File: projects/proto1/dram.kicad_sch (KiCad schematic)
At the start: 21 parts, among them J1 ATRANS, U10 DP8440, U11 74LS245, U5 74LS245, U6 SIMM72, U7 SIMM72, U8 74LS245, U9 74LS245

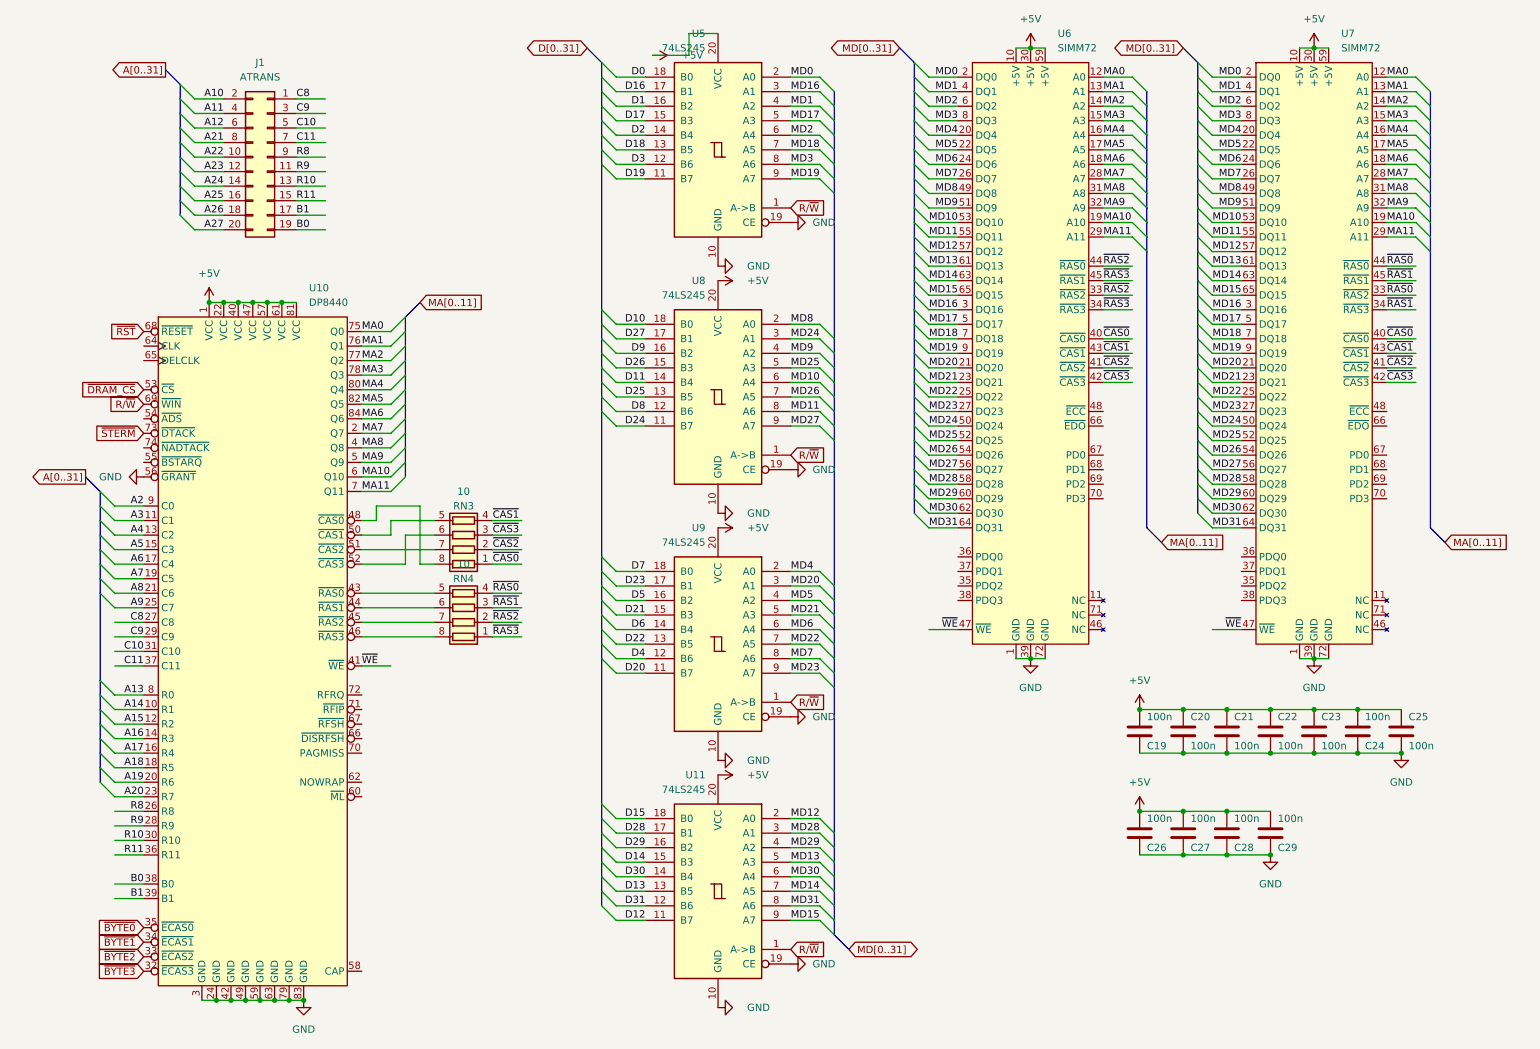
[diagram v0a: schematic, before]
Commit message: Renamed CMC to SCU, changed verification method to cocotb, and modified pcb schematic
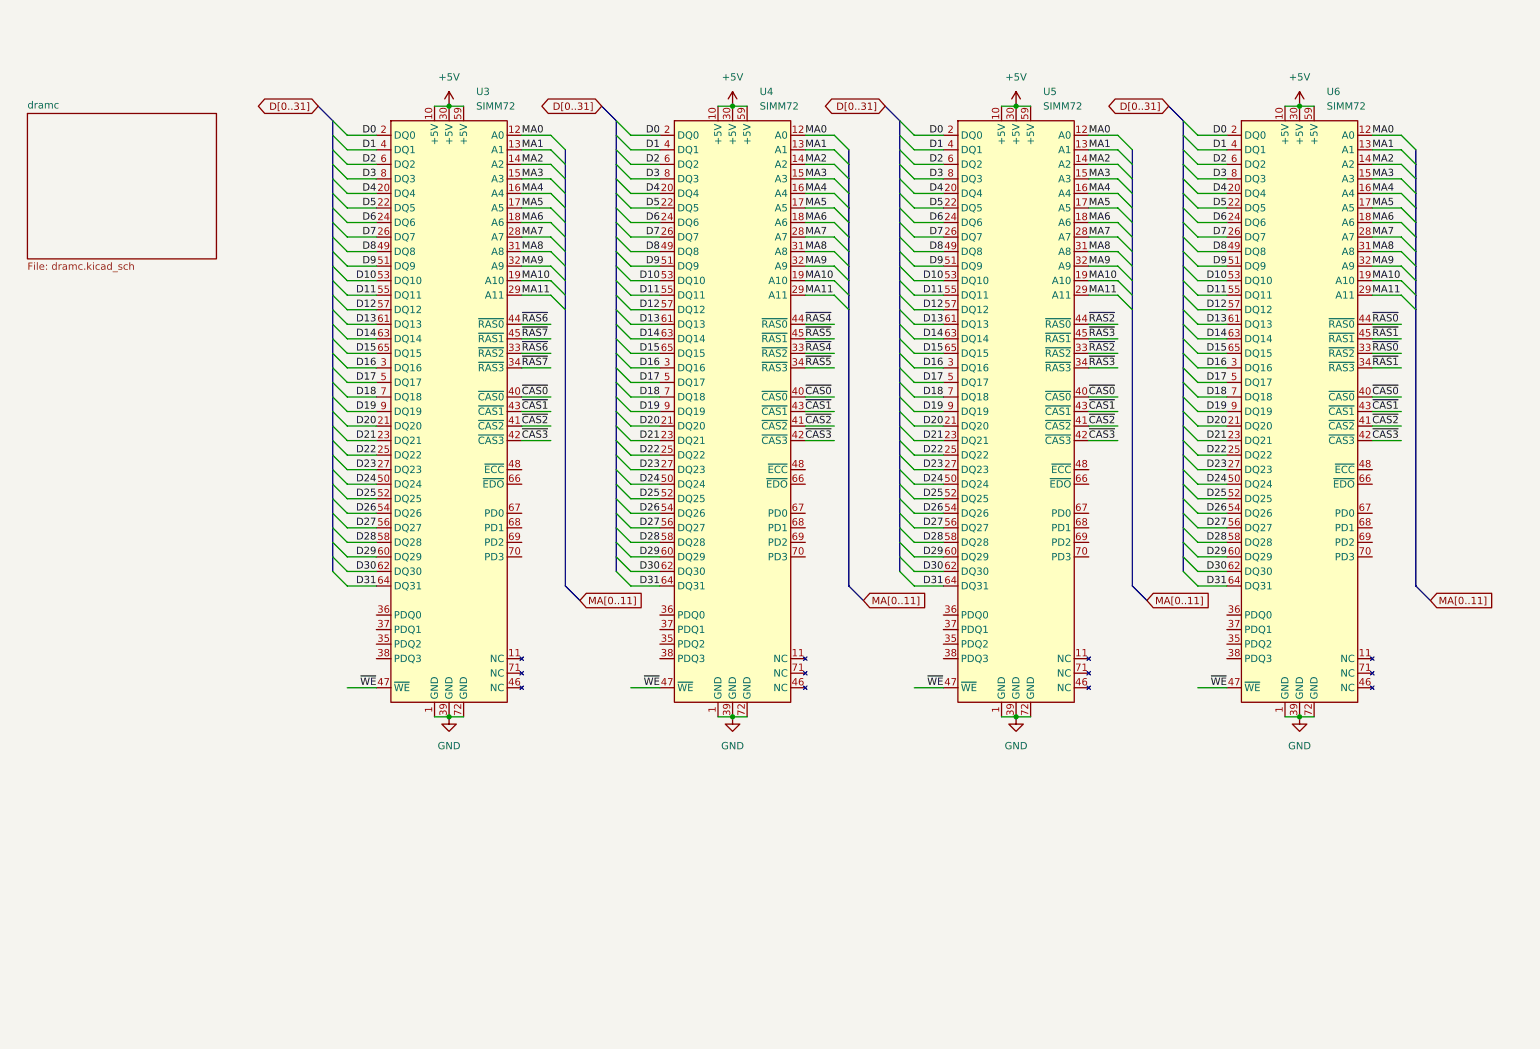
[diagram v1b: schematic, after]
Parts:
- removed C19, C20, C21, C22, C23, C24, C25, C26, C27, C28, C29: 100n, Capacitor_THT:C_Disc_D4.3mm_W1.9mm_P5.00mm, symbol Device:C
- removed J1: ATRANS, Connector_PinHeader_2.54mm:PinHeader_2x10_P2.54mm_Vertical, symbol Connector_Generic:Conn_02x10_Odd_Even
- removed RN3, RN4: 10, Package_DIP:DIP-8_W7.62mm, symbol Device:R_Pack04
- removed U10: DP8440, Package_LCC:PLCC-84_THT-Socket, symbol m68k-hbc-ic:DP8440
- removed U11, U5, U8, U9: 74LS245, Package_DIP:DIP-20_W7.62mm_Socket, symbol 74xx:74LS245
- added U5, U6: SIMM72, m68k-hbc-conn:SIMM72, symbol m68k-hbc-conn:SIMM72
- renumbered U6 to U3, U7 to U4
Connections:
- net MD0 is gone; now on net D0: U3.2 (DQ0), U4.2 (DQ0)
- net MD1 is gone; now on net D1: U3.4 (DQ1), U4.4 (DQ1)
- net MD10 is gone; now on net D10: U3.53 (DQ10), U4.53 (DQ10)
- net MD11 is gone; now on net D11: U3.55 (DQ11), U4.55 (DQ11)
- net MD12 is gone; now on net D12: U3.57 (DQ12), U4.57 (DQ12)
- net MD13 is gone; now on net D13: U3.61 (DQ13), U4.61 (DQ13)
- net MD14 is gone; now on net D14: U3.63 (DQ14), U4.63 (DQ14)
- net MD15 is gone; now on net D15: U3.65 (DQ15), U4.65 (DQ15)
- net MD16 is gone; now on net D16: U3.3 (DQ16), U4.3 (DQ16)
- net MD17 is gone; now on net D17: U3.5 (DQ17), U4.5 (DQ17)
- net MD18 is gone; now on net D18: U3.7 (DQ18), U4.7 (DQ18)
- net MD19 is gone; now on net D19: U3.9 (DQ19), U4.9 (DQ19)
- net MD2 is gone; now on net D2: U3.6 (DQ2), U4.6 (DQ2)
- net MD20 is gone; now on net D20: U3.21 (DQ20), U4.21 (DQ20)
- net MD21 is gone; now on net D21: U3.23 (DQ21), U4.23 (DQ21)
- net MD22 is gone; now on net D22: U3.25 (DQ22), U4.25 (DQ22)
- net MD23 is gone; now on net D23: U3.27 (DQ23), U4.27 (DQ23)
- net MD24 is gone; now on net D24: U3.50 (DQ24), U4.50 (DQ24)
- net MD25 is gone; now on net D25: U3.52 (DQ25), U4.52 (DQ25)
- net MD26 is gone; now on net D26: U3.54 (DQ26), U4.54 (DQ26)
- net MD27 is gone; now on net D27: U3.56 (DQ27), U4.56 (DQ27)
- net MD28 is gone; now on net D28: U3.58 (DQ28), U4.58 (DQ28)
- net MD29 is gone; now on net D29: U3.60 (DQ29), U4.60 (DQ29)
- net MD3 is gone; now on net D3: U3.8 (DQ3), U4.8 (DQ3)
- net MD30 is gone; now on net D30: U3.62 (DQ30), U4.62 (DQ30)
- net MD31 is gone; now on net D31: U3.64 (DQ31), U4.64 (DQ31)
- net MD4 is gone; now on net D4: U3.20 (DQ4), U4.20 (DQ4)
- net MD5 is gone; now on net D5: U3.22 (DQ5), U4.22 (DQ5)
- net MD6 is gone; now on net D6: U3.24 (DQ6), U4.24 (DQ6)
- net MD7 is gone; now on net D7: U3.26 (DQ7), U4.26 (DQ7)
- net MD8 is gone; now on net D8: U3.49 (DQ8), U4.49 (DQ8)
- net MD9 is gone; now on net D9: U3.51 (DQ9), U4.51 (DQ9)
- net +5V: now also U5.10 (+5V), U5.30 (+5V), U5.59 (+5V), U6.10 (+5V), U6.30 (+5V), U6.59 (+5V)
- net D0: now also U5.2 (DQ0), U6.2 (DQ0)
- net D1: now also U5.4 (DQ1), U6.4 (DQ1)
- net D10: now also U5.53 (DQ10), U6.53 (DQ10)
- net D11: now also U5.55 (DQ11), U6.55 (DQ11)
- net D12: now also U5.57 (DQ12), U6.57 (DQ12)
- net D13: now also U5.61 (DQ13), U6.61 (DQ13)
- net D14: now also U5.63 (DQ14), U6.63 (DQ14)
- net D15: now also U5.65 (DQ15), U6.65 (DQ15)
- net D16: now also U5.3 (DQ16), U6.3 (DQ16)
- net D17: now also U5.5 (DQ17), U6.5 (DQ17)
- net D18: now also U5.7 (DQ18), U6.7 (DQ18)
- net D19: now also U5.9 (DQ19), U6.9 (DQ19)
- net D2: now also U5.6 (DQ2), U6.6 (DQ2)
- net D20: now also U5.21 (DQ20), U6.21 (DQ20)
- net D21: now also U5.23 (DQ21), U6.23 (DQ21)
- net D22: now also U5.25 (DQ22), U6.25 (DQ22)
- net D23: now also U5.27 (DQ23), U6.27 (DQ23)
- net D24: now also U5.50 (DQ24), U6.50 (DQ24)
- net D25: now also U5.52 (DQ25), U6.52 (DQ25)
- net D26: now also U5.54 (DQ26), U6.54 (DQ26)
- net D27: now also U5.56 (DQ27), U6.56 (DQ27)
- net D28: now also U5.58 (DQ28), U6.58 (DQ28)
- net D29: now also U5.60 (DQ29), U6.60 (DQ29)
- net D3: now also U5.8 (DQ3), U6.8 (DQ3)
- net D30: now also U5.62 (DQ30), U6.62 (DQ30)
- net D31: now also U5.64 (DQ31), U6.64 (DQ31)
- net D4: now also U5.20 (DQ4), U6.20 (DQ4)
- net D5: now also U5.22 (DQ5), U6.22 (DQ5)
- net D6: now also U5.24 (DQ6), U6.24 (DQ6)
- net D7: now also U5.26 (DQ7), U6.26 (DQ7)
- net D8: now also U5.49 (DQ8), U6.49 (DQ8)
- net D9: now also U5.51 (DQ9), U6.51 (DQ9)
- net GND: now also U5.1 (GND), U5.39 (GND), U5.72 (GND), U6.1 (GND), U6.39 (GND), U6.72 (GND)
- net MA0: now also U5.12 (A0), U6.12 (A0)
- net MA1: now also U5.13 (A1), U6.13 (A1)
- net MA10: now also U5.19 (A10), U6.19 (A10)
- net MA11: now also U5.29 (A11), U6.29 (A11)
- net MA2: now also U5.14 (A2), U6.14 (A2)
- net MA3: now also U5.15 (A3), U6.15 (A3)
- net MA4: now also U5.16 (A4), U6.16 (A4)
- net MA5: now also U5.17 (A5), U6.17 (A5)
- net MA6: now also U5.18 (A6), U6.18 (A6)
- net MA7: now also U5.28 (A7), U6.28 (A7)
- net MA8: now also U5.31 (A8), U6.31 (A8)
- net MA9: now also U5.32 (A9), U6.32 (A9)
- net ~{CAS0}: now also U5.40 (~{CAS0}), U6.40 (~{CAS0})
- net ~{CAS1}: now also U5.43 (~{CAS1}), U6.43 (~{CAS1})
- net ~{CAS2}: now also U5.41 (~{CAS2}), U6.41 (~{CAS2})
- net ~{CAS3}: now also U5.42 (~{CAS3}), U6.42 (~{CAS3})
- net ~{RAS0}: now also U6.33 (~{RAS2}), U6.44 (~{RAS0}); no longer U4.33 (~{RAS2}), U4.44 (~{RAS0})
- net ~{RAS1}: now also U6.34 (~{RAS3}), U6.45 (~{RAS1}); no longer U4.34 (~{RAS3}), U4.45 (~{RAS1})
- net ~{RAS2}: now also U5.33 (~{RAS2}), U5.44 (~{RAS0}); no longer U3.33 (~{RAS2}), U3.44 (~{RAS0})
- net ~{RAS3}: now also U5.34 (~{RAS3}), U5.45 (~{RAS1}); no longer U3.34 (~{RAS3}), U3.45 (~{RAS1})
- net ~{WE}: now also U5.47 (~{WE}), U6.47 (~{WE})
- new net ~{RAS4}: U4.33 (~{RAS2}), U4.44 (~{RAS0})
- new net ~{RAS5}: U4.34 (~{RAS3}), U4.45 (~{RAS1})
- new net ~{RAS6}: U3.33 (~{RAS2}), U3.44 (~{RAS0})
- new net ~{RAS7}: U3.34 (~{RAS3}), U3.45 (~{RAS1})
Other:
- added sheet dramc (dramc.kicad_sch)
- moved on the sheet: U3, U4
